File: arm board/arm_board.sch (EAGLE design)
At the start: 97 parts, among them J1 APPPP45_PCB_HORIZ_RIGHT, J14 APPPP45_PCB_HORIZ_RIGHT, J15 APPPP45_PCB_HORIZ_RIGHT, J16 APPPP45_PCB_HORIZ_RIGHT, J17 APPPP45_PCB_HORIZ_RIGHT, J18 APPPP45_PCB_HORIZ_RIGHT, J19 ENCODER, J2 APPPP45_PCB_HORIZ_RIGHT, J20 ENCODER, J21 ENCODER, J22 ENCODER, J24 ENCODER, J3 APPPP45_PCB_HORIZ_RIGHT, Q1 Q_IRF7437SMD, U1 TIVA-1294, U3 MAX3232D

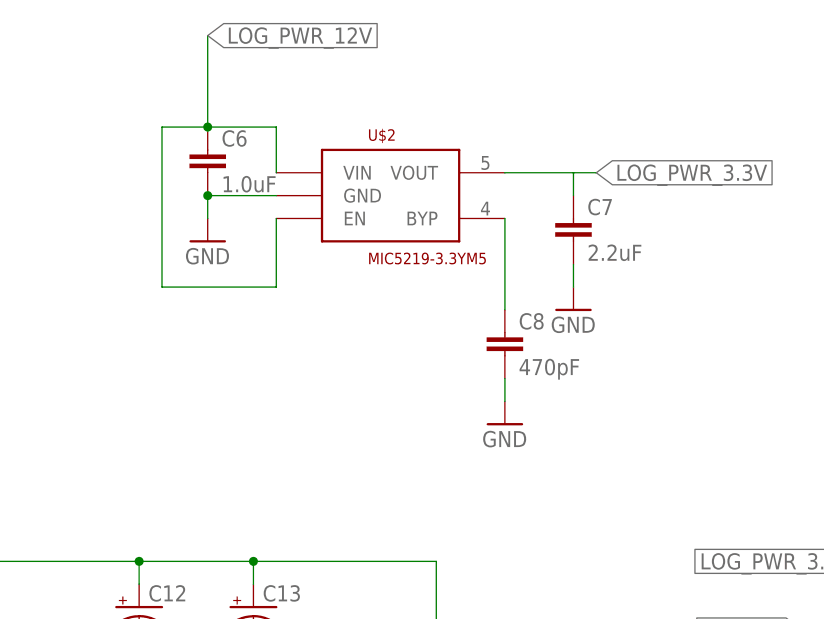
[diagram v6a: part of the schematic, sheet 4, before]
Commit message: Added new lin reg IC to power tiva
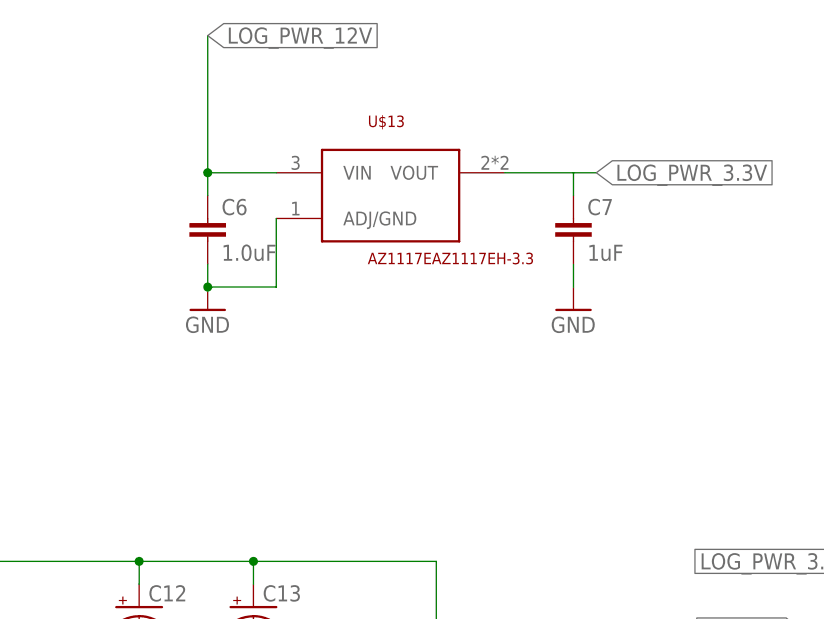
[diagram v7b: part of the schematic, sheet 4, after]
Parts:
- removed C8: 470pF, SparkFun-Capacitors:0.1UF-25V(+80/-20%)(0603)
- removed U$2: MIC5219-3.3YM5, MRDT-ICs:MIC5219-3.3YM5
- added U$13: AZ1117EAZ1117EH-3.3, MRDT-ICs:AZ1117EAZ1117EH-3.3
- C7: value 2.2uF -> 1uF
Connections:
- removed net N$2: C8.1, U$2.BYP
- net GND: now also U$13.ADJ/GND; no longer C8.2, U$2.GND
- net LOG_PWR_12V: now also U$13.VIN; no longer U$2.EN, U$2.VIN
- net LOG_PWR_3.3V: now also U$13.VOUT; no longer U$2.VOUT
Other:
- moved on the sheet: C6
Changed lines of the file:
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@@
 <part name="C55" library="SparkFun-Capacitors" deviceset="0.1UF-25V(+80/-20%)(0603)" device="" value=".01uF"/>
 <part name="GND63" library="SparkFun-Aesthetics" deviceset="GND" device=""/>
-<part name="U$2" library="MRDT-ICs" deviceset="MIC5219-3.3YM5" device=""/>
 <part name="GND19" library="SparkFun-Aesthetics" deviceset="GND" device=""/>
 <part name="C6" library="SparkFun-Capacitors" deviceset="1.0UF-16V-10%(0603)" device="" value="1.0uF"/>
-<part name="C7" library="SparkFun-Capacitors" deviceset="0.1UF-25V(+80/-20%)(0603)" device="" value="2.2uF"/>
-<part name="C8" library="SparkFun-Capacitors" deviceset="0.1UF-25V(+80/-20%)(0603)" device="" value="470pF"/>
+<part name="C7" library="SparkFun-Capacitors" deviceset="0.1UF-25V(+80/-20%)(0603)" device="" value="1uF"/>
 <part name="GND20" library="SparkFun-Aesthetics" deviceset="GND" device=""/>
-<part name="GND21" library="SparkFun-Aesthetics" deviceset="GND" device=""/>
 <part name="U1" library="MRDT-Microcontrollers" deviceset="TIVA-1294" device=""/>
 <part name="GND12" library="SparkFun-Aesthetics" deviceset="GND" device=""/>
@@
 <part name="C13" library="SparkFun-Capacitors" deviceset="CAP_POL" device="E" value="330uF"/>
 <part name="C12" library="SparkFun-Capacitors" deviceset="CAP_POL" device="E" value="330uF"/>
+<part name="U$13" library="MRDT-ICs" deviceset="AZ1117E" device="AZ1117EH-3.3"/>
 </parts>
 <sheets>
@@
 </plain>
 <instances>
-<instance part="U$2" gate="G$1" x="-25.4" y="38.1"/>
-<instance part="GND19" gate="1" x="-45.72" y="33.02"/>
-<instance part="C6" gate="G$1" x="-45.72" y="40.64"/>
+<instance part="GND19" gate="1" x="-45.72" y="25.4"/>
+<instance part="C6" gate="G$1" x="-45.72" y="33.02"/>
 <instance part="C7" gate="G$1" x="-5.08" y="33.02"/>
-<instance part="C8" gate="G$1" x="-12.7" y="20.32"/>
 <instance part="GND20" gate="1" x="-5.08" y="25.4"/>
-<instance part="GND21" gate="1" x="-12.7" y="12.7"/>
 <instance part="U$0" gate="G$1" x="-2.54" y="-73.66"/>
 <instance part="C3" gate="G$1" x="-22.86" y="-81.28"/>
@@
 <instance part="C13" gate="G$1" x="-40.64" y="-7.62"/>
 <instance part="C12" gate="G$1" x="-53.34" y="-7.62"/>
+<instance part="U$13" gate="G$1" x="-25.4" y="33.02"/>
 </instances>
 <busses>
@@
 <net name="GND" class="0">
 <segment>
-<pinref part="U$2" gate="G$1" pin="GND"/>
-<wire x1="-38.1" y1="38.1" x2="-45.72" y2="38.1" width="0.1524" layer="91"/>
-<wire x1="-45.72" y1="38.1" x2="-45.72" y2="35.56" width="0.1524" layer="91"/>
+<wire x1="-45.72" y1="30.48" x2="-45.72" y2="27.94" width="0.1524" layer="91"/>
 <pinref part="GND19" gate="1" pin="GND"/>
 <pinref part="C6" gate="G$1" pin="2"/>
-<junction x="-45.72" y="38.1"/>
+<pinref part="U$13" gate="G$1" pin="ADJ/GND"/>
+<wire x1="-38.1" y1="35.56" x2="-38.1" y2="27.94" width="0.1524" layer="91"/>
+<wire x1="-38.1" y1="27.94" x2="-45.72" y2="27.94" width="0.1524" layer="91"/>
+<junction x="-45.72" y="27.94"/>
 </segment>
 <segment>
@@
 <pinref part="GND20" gate="1" pin="GND"/>
 <wire x1="-5.08" y1="27.94" x2="-5.08" y2="30.48" width="0.1524" layer="91"/>
-</segment>
-<segment>
-<pinref part="C8" gate="G$1" pin="2"/>
-<pinref part="GND21" gate="1" pin="GND"/>
-<wire x1="-12.7" y1="15.24" x2="-12.7" y2="17.78" width="0.1524" layer="91"/>
 </segment>
 <segment>
@@
 <net name="LOG_PWR_12V" class="0">
 <segment>
-<wire x1="-45.72" y1="45.72" x2="-45.72" y2="55.88" width="0.1524" layer="91"/>
-<pinref part="U$2" gate="G$1" pin="VIN"/>
-<wire x1="-38.1" y1="40.64" x2="-38.1" y2="45.72" width="0.1524" layer="91"/>
-<wire x1="-38.1" y1="45.72" x2="-45.72" y2="45.72" width="0.1524" layer="91"/>
+<wire x1="-45.72" y1="38.1" x2="-45.72" y2="40.64" width="0.1524" layer="91"/>
 <label x="-45.72" y="55.88" size="1.778" layer="95" xref="yes"/>
-<pinref part="U$2" gate="G$1" pin="EN"/>
-<wire x1="-38.1" y1="35.56" x2="-38.1" y2="27.94" width="0.1524" layer="91"/>
-<wire x1="-38.1" y1="27.94" x2="-50.8" y2="27.94" width="0.1524" layer="91"/>
-<wire x1="-50.8" y1="27.94" x2="-50.8" y2="45.72" width="0.1524" layer="91"/>
-<wire x1="-50.8" y1="45.72" x2="-45.72" y2="45.72" width="0.1524" layer="91"/>
 <pinref part="C6" gate="G$1" pin="1"/>
-<junction x="-45.72" y="45.72"/>
+<pinref part="U$13" gate="G$1" pin="VIN"/>
+<wire x1="-45.72" y1="40.64" x2="-45.72" y2="55.88" width="0.1524" layer="91"/>
+<wire x1="-38.1" y1="40.64" x2="-45.72" y2="40.64" width="0.1524" layer="91"/>
+<junction x="-45.72" y="40.64"/>
 </segment>
 </net>
@@
 <label x="-2.54" y="40.64" size="1.778" layer="95" xref="yes"/>
 <pinref part="C7" gate="G$1" pin="1"/>
-<pinref part="U$2" gate="G$1" pin="VOUT"/>
 <wire x1="-12.7" y1="40.64" x2="-5.08" y2="40.64" width="0.1524" layer="91"/>
 <wire x1="-2.54" y1="40.64" x2="-5.08" y2="40.64" width="0.1524" layer="91"/>
 <wire x1="-5.08" y1="40.64" x2="-5.08" y2="38.1" width="0.1524" layer="91"/>
+<pinref part="U$13" gate="G$1" pin="VOUT"/>
 </segment>
 <segment>
@@
 </segment>
 </net>
-<net name="N$2" class="0">
-<segment>
-<pinref part="U$2" gate="G$1" pin="BYP"/>
-<pinref part="C8" gate="G$1" pin="1"/>
-<wire x1="-12.7" y1="25.4" x2="-12.7" y2="35.56" width="0.1524" layer="91"/>
-</segment>
-</net>
